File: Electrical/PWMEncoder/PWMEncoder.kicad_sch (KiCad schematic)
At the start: 1 part, among them U1 ATMEGA32U4-AU

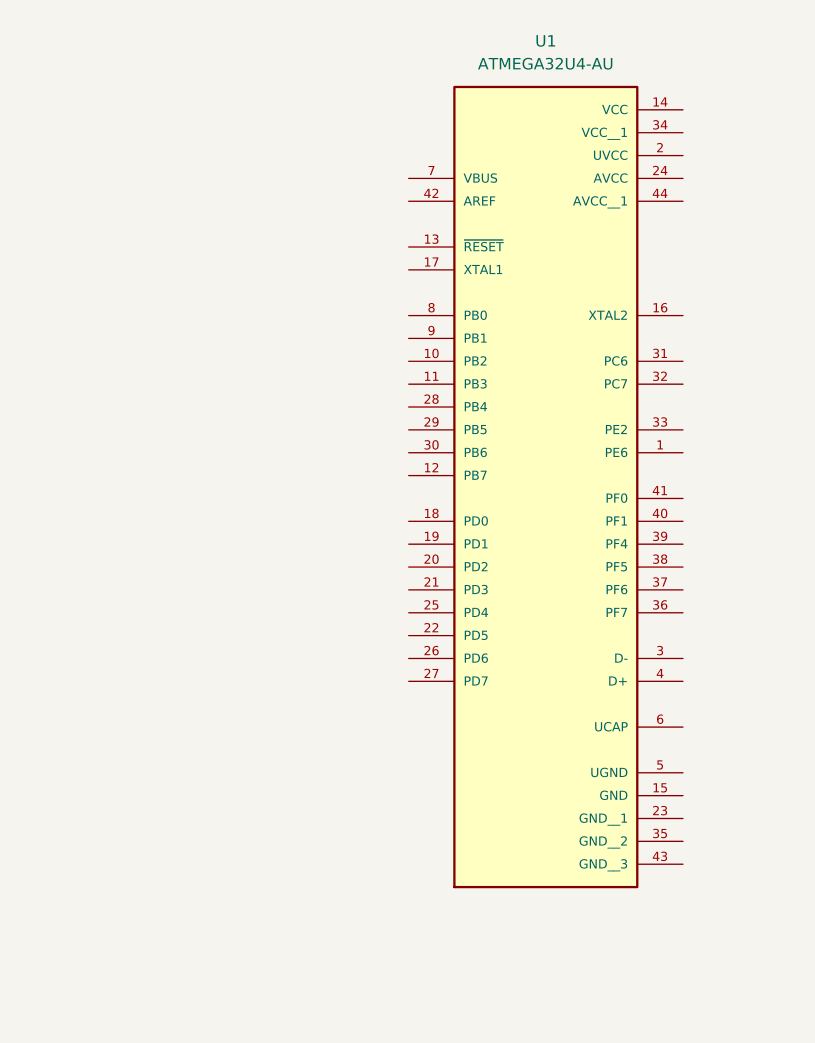
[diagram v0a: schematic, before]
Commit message: Started PWM Encoder PCB
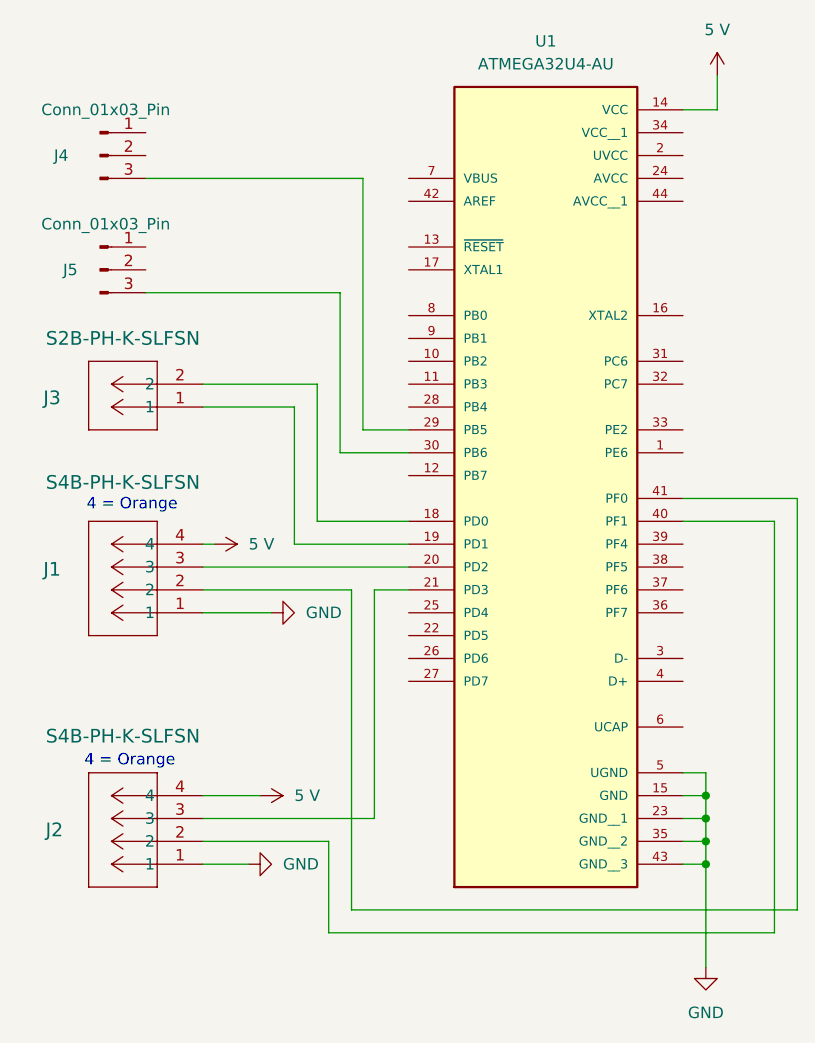
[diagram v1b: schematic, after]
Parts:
- added J1, J2: S4B-PH-K-SLFSN, CONN_S4B-PH-K-S_JST, symbol jst_ph_4pin_horizontal:S4B-PH-K-SLFSN
- added J3: S2B-PH-K-SLFSN, CONN_S2B-PH-K-S_JST, symbol jxt_ph_2pin_horizontal:S2B-PH-K-SLFSN
- added J4, J5: Conn_01x03_Pin, symbol Connector:Conn_01x03_Pin
- U1: footprint ATMEGA32U4-AU:QFP80P1200X1200X120-44N -> Footprints2:QFP80P1200X1200X120-44N
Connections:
- net 5 V: now reaches U1.14 (VCC)
- net 5 V: now also J1.4, J2.4
- net GND: now reaches U1.15 (GND)
- net GND: now also U1.23 (GND__1), U1.35 (GND__2), U1.43 (GND__3), U1.5 (UGND), J1.1, J2.1
- net at U1.18 (PD0): now also J3.2
- net at U1.19 (PD1): now also J3.1
- net at U1.20 (PD2): now also J1.3
- net at U1.21 (PD3): now also J2.3
- net at U1.29 (PB5): now also J4.3 (Pin_3)
- net at U1.30 (PB6): now also J5.3 (Pin_3)
- net at U1.40 (PF1): now also J2.2
- net at U1.41 (PF0): now also J1.2
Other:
- note added: "4 = Orange"
